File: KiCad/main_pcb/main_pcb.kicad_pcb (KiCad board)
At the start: 2 copper layers, 130 x 100 mm, 57 parts, among them J1 Conn_01x07, J2 Conn_01x07, J3 Conn_01x13, J4 Conn_01x06, J5 Conn_01x02, J6 USB_C_Receptacle_USB2.0_14P, SW1 SW_Push, U1 TXB0104D, U2 TXB0104D, U3 TXB0104D, U4 ATmega2560-16A, U5 AMS1117-3.3, U7 CH340C, Y1 Crystal_GND24

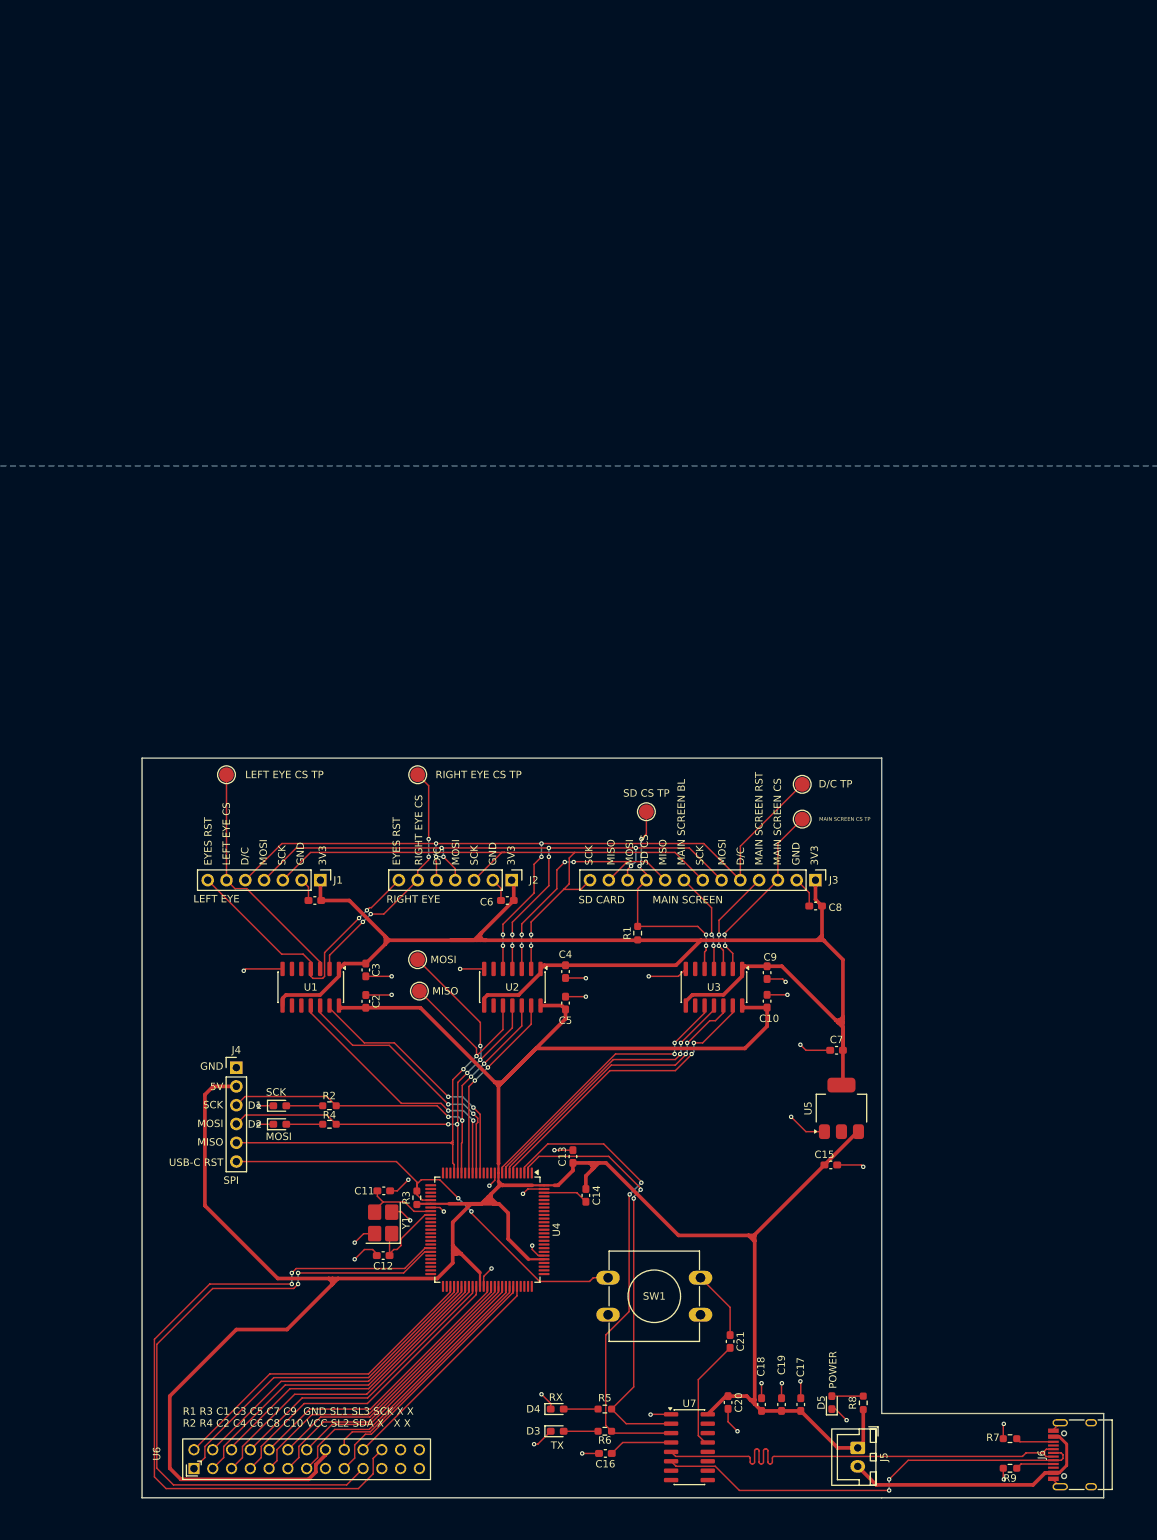
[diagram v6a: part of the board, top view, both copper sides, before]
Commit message: chore(migration): Migrates to homebrew symbols for PCB.
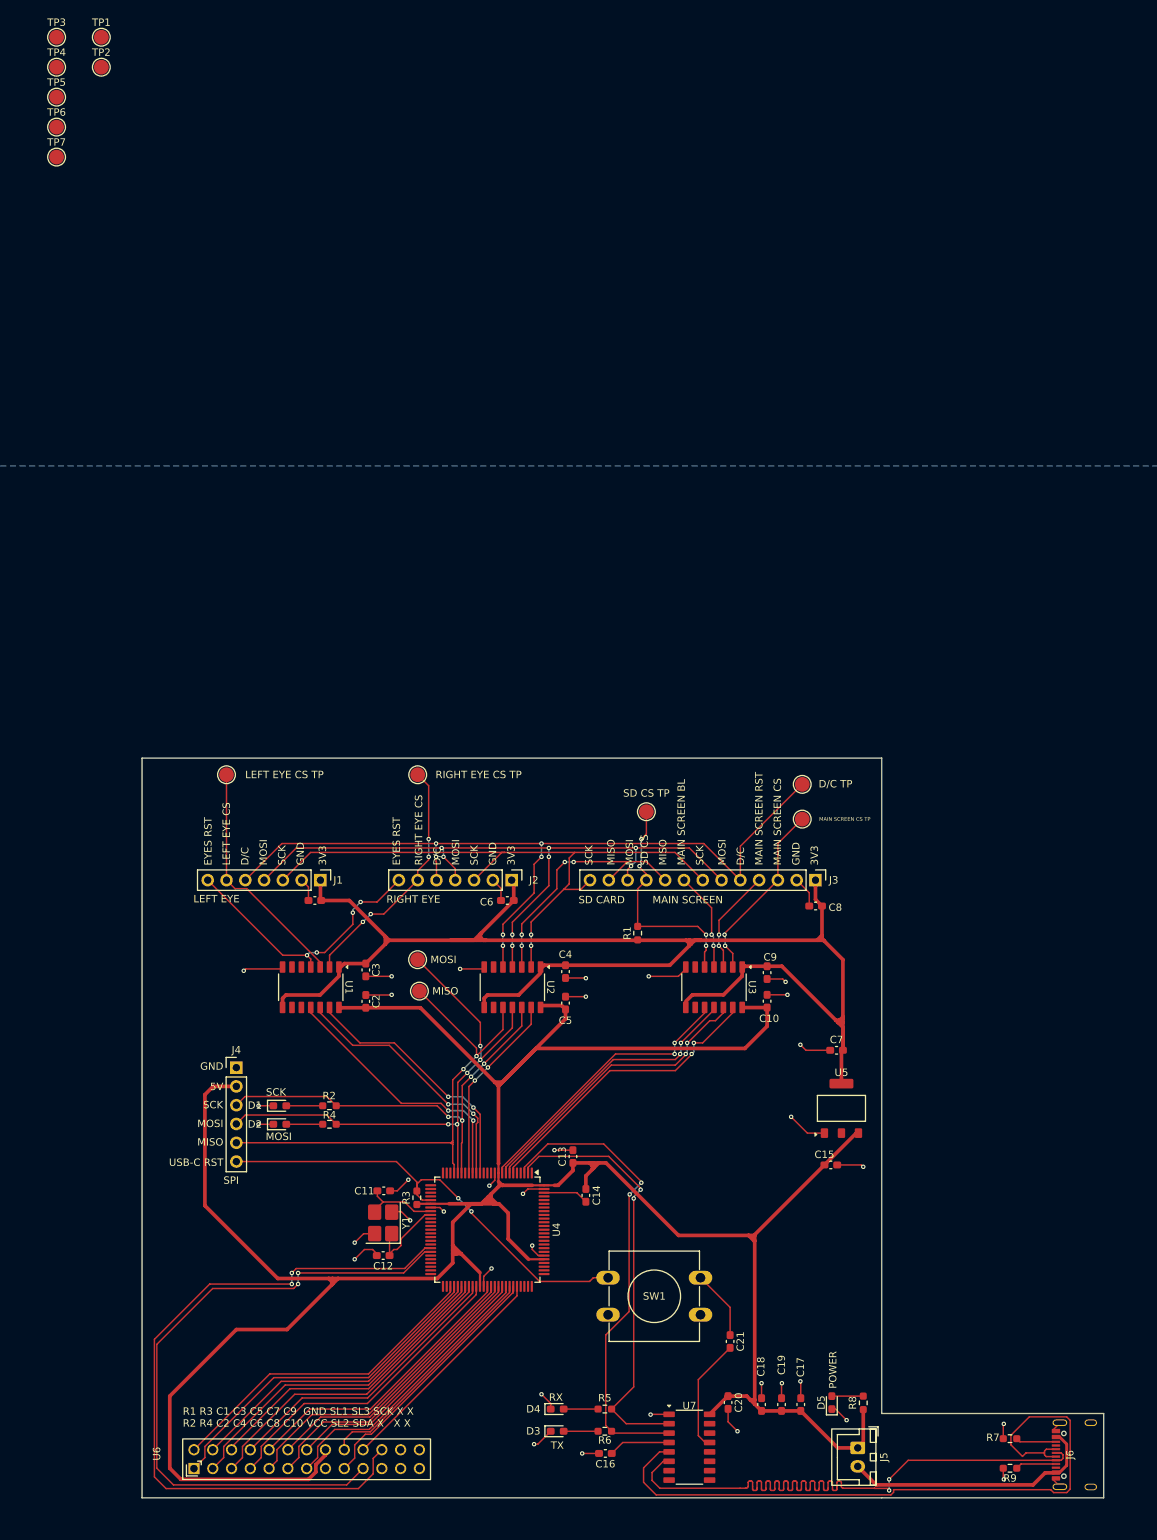
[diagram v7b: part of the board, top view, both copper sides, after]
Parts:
- added TP1: TestPoint, TestPoint:TestPoint_Pad_D2.0mm, F.Cu at (37.5, -52.0)
- added TP2: TestPoint, TestPoint:TestPoint_Pad_D2.0mm, F.Cu at (37.5, -47.9)
- added TP3: Test SD CS, TestPoint:TestPoint_Pad_D2.0mm, F.Cu at (31.4, -52.0)
- added TP4: Test Right Eye CS, TestPoint:TestPoint_Pad_D2.0mm, F.Cu at (31.4, -47.9)
- added TP5: Test Left Eye CS, TestPoint:TestPoint_Pad_D2.0mm, F.Cu at (31.4, -43.9)
- added TP6: Test Main Screen CS, TestPoint:TestPoint_Pad_D2.0mm, F.Cu at (31.4, -39.8)
- added TP7: Test DC, TestPoint:TestPoint_Pad_D2.0mm, F.Cu at (31.4, -35.8)
- J6: footprint Connector_USB:USB_C_Receptacle_HRO_TYPE-C-31-M-12 -> Lilibrary:USB-C (Home-brew)
- U1, U2, U3: footprint Package_SO:SOIC-14_3.9x8.7mm_P1.27mm -> Lilibrary:SOIC-14_TXB0104DR
- U5: footprint Package_TO_SOT_SMD:SOT-223-3_TabPin2 -> Lilibrary:SOT-223-3_TabPin2_AMS1117
- U7: footprint Package_SO:SOIC-16_3.9x9.9mm_P1.27mm -> Lilibrary:SOP-16_CH340C
- turned U5 to 0 degrees
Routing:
- net /USB-C/D+: track 62.7 -> 93.9 mm
- net /USB-C/D-: track 59.2 -> 88.6 mm
- net /Screens/EYES_RST-3V3: track 39.9 -> 37.5 mm, vias 2 -> 4
- net 3V3: track 205.4 -> 207.5 mm

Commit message: feat(pcb): I think that's about right
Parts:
- removed D/C TP: Test DC, TestPoint:TestPoint_Pad_D2.0mm
- removed LEFT EYE CS TP: Test Left Eye CS, TestPoint:TestPoint_Pad_D2.0mm
- removed MAIN SCREEN CS TP: Test Main Screen CS, TestPoint:TestPoint_Pad_D2.0mm
- removed MISO, MOSI: TestPoint, TestPoint:TestPoint_Pad_D2.0mm
- removed RIGHT EYE CS TP: Test Right Eye CS, TestPoint:TestPoint_Pad_D2.0mm
- removed SD CS TP: Test SD CS, TestPoint:TestPoint_Pad_D2.0mm
- added REF**: Mounting_Hole_3.2mm_M3, Lilibrary:Mounting_Hole_3.2mm_M3, F.Cu at (47.2, 115.3)
- added REF**: Mounting_Hole_3.2mm_M3, Lilibrary:Mounting_Hole_3.2mm_M3, F.Cu at (134.3, 115.3)
- added REF**: Mounting_Hole_3.2mm_M3, Lilibrary:Mounting_Hole_3.2mm_M3, F.Cu at (47.2, 54.2)
- added REF**: Mounting_Hole_3.2mm_M3, Lilibrary:Mounting_Hole_3.2mm_M3, F.Cu at (139.6, 54.2)
- C1, C10, C11, C12, C13, C14, C15, C16, C17, C18, C19, C2, C20, C21, C3, C4, C5, C6, C7, C8, C9: footprint Capacitor_SMD:C_0603_1608Metric_Pad1.08x0.95mm_HandSolder -> Lilibrary:Capacitor_0603
- D1, D2, D3, D4, D5: footprint LED_SMD:LED_0603_1608Metric_Pad1.05x0.95mm_HandSolder -> Lilibrary:LED_0603
- J6: footprint Lilibrary:USB-C (Home-brew) -> Lilibrary:USB_C_Receptacle_HRO_TYPE-C-31-M-12
- R1, R2, R3, R4, R5, R6, R7, R8, R9: footprint Resistor_SMD:R_0603_1608Metric_Pad0.98x0.95mm_HandSolder -> Lilibrary:Resistor_0603
- SW1: footprint Button_Switch_THT:SW_PUSH-12mm -> Lilibrary:Switch_Push_Button_12mm
- TP1, TP2, TP3, TP4, TP5, TP6, TP7: footprint TestPoint:TestPoint_Pad_D2.0mm -> Lilibrary:Test point
- moved TP6 137.5 mm to (132.2, 53.8)
- moved TP2 132.1 mm to (80.5, 77.0)
- moved TP1 131.8 mm to (80.2, 72.8)
- moved TP7 131.7 mm to (132.2, 49.0)
- moved TP3 131.6 mm to (111.2, 52.8)
- moved TP4 107.4 mm to (80.3, 47.8)
- moved TP5 94.4 mm to (54.4, 47.8)
- moved SW1 6.79 mm to (112.2, 118.4)
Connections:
- J6 pad S2: (no net) -> GND
- J6 pad S3: (no net) -> GND
- J6 pad S4: (no net) -> GND
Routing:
- net 3V3: track 207.5 -> 216.7 mm
- net /Screens/LEFT_EYE_CS-3V3: track 33.4 -> 31.5 mm
- net Net-(U7-~{DTR}): track 15.0 -> 16.1 mm
- net /USB-C/D+: track 93.9 -> 95.0 mm
- net /Screens/SD_CS: track 38.7 -> 37.6 mm
- net /Screens/Left_Eye_CS: track 35.7 -> 34.7 mm
- net /Screens/Eyes_RST: track 36.1 -> 35.1 mm
- net Net-(J6-CC2): track 5.13 -> 6.09 mm
- net /Screens/Main_Screen_LED/BL: track 38.7 -> 39.5 mm
- net /Screens/Main_Screen_RST: track 40.3 -> 39.5 mm
- net /Screens/Right_Eye_CS: track 34.6 -> 34.0 mm
- net VCC: track 398.1 -> 397.5 mm
- net /USB-C/D-: track 88.6 -> 89.1 mm
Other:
- board text added: "D/C TP"
- board text added: "LEFT EYE CS TP"
- board text added: "MAIN SCREEN CS TP"
- board text added: "RIGHT EYE CS TP"
- board text added: "SD CS TP"
